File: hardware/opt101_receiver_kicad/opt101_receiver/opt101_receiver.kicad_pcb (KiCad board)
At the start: 2 copper layers, 70 x 32 mm, 11 parts, among them J1 A2 / RED, J2 A0 / IR, J3 ADS1115 outputs, U1 OPT101P, U2 OPT101P

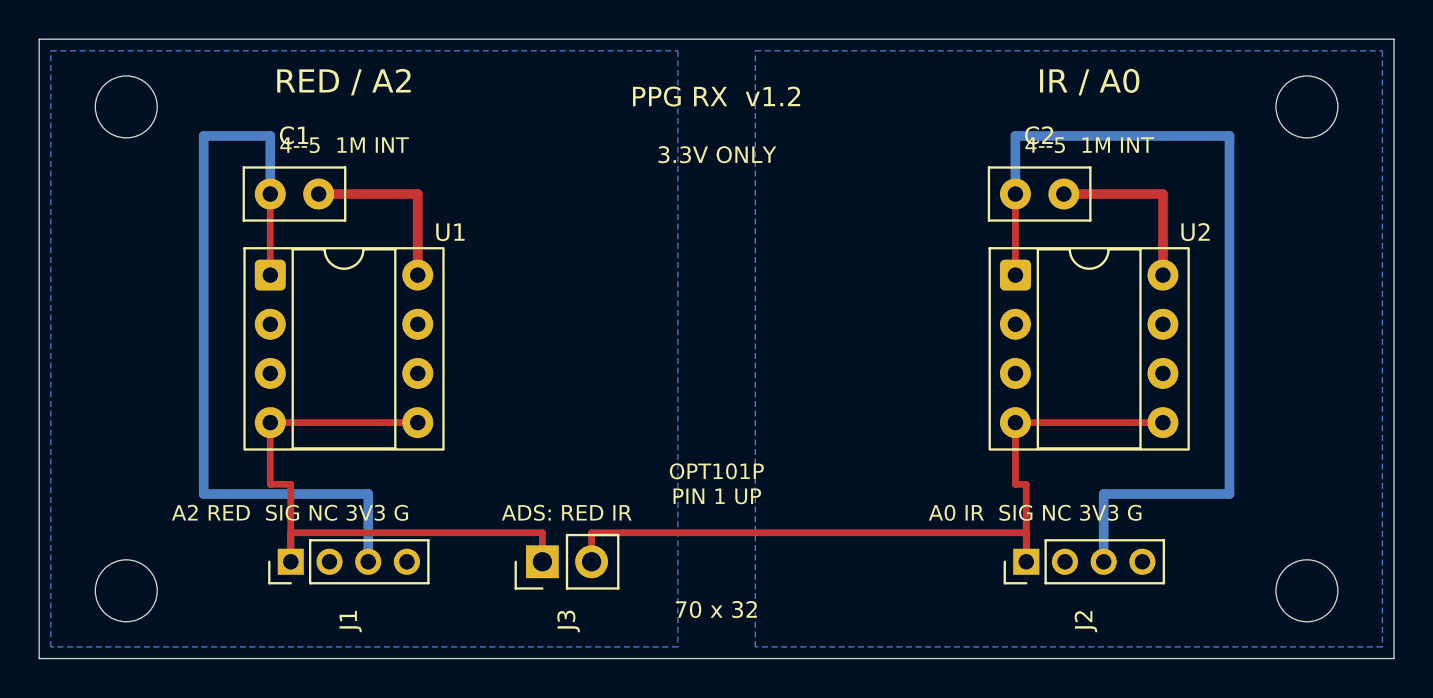
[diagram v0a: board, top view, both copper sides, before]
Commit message: Compact PPG boards, add receiver filters and package V-cut panel
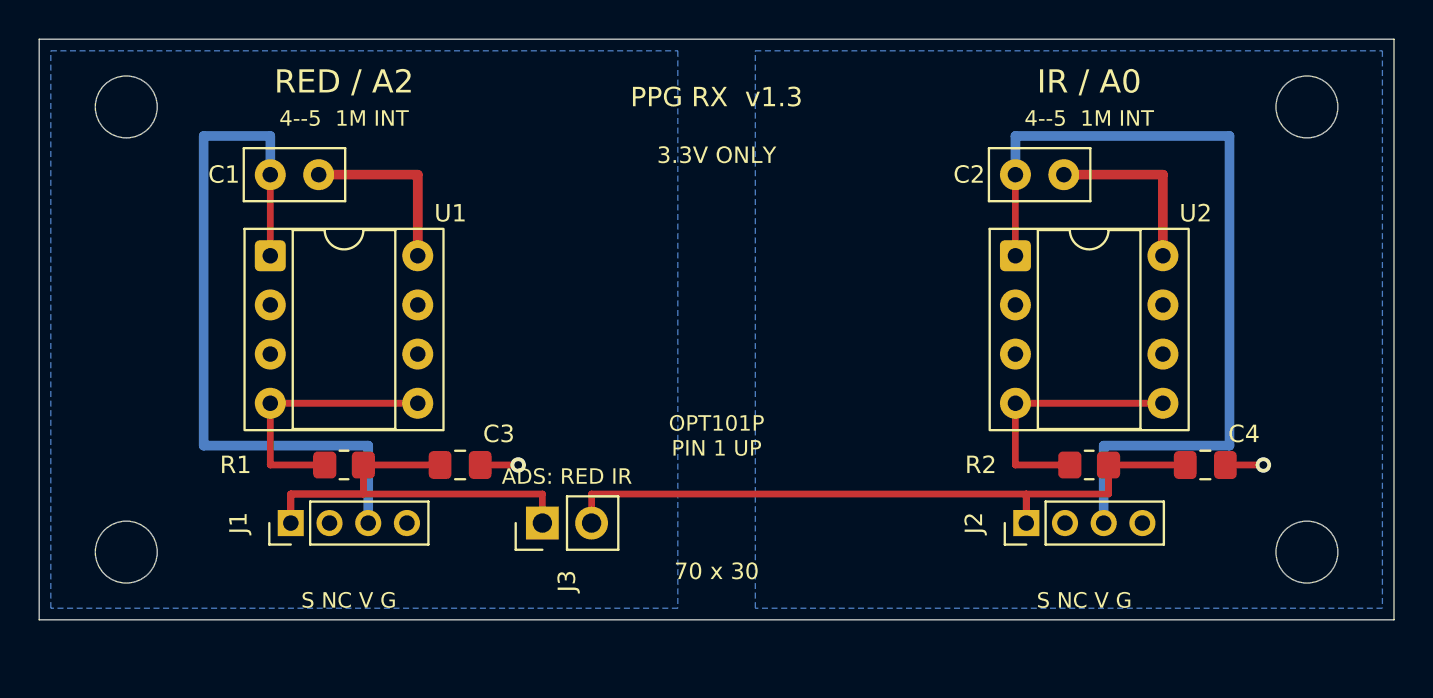
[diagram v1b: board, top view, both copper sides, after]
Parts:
- added C3: 1uF X7R 16V, PPG:C0805_Hand, F.Cu at (121.8, 122.0)
- added C4: 1uF X7R 16V, PPG:C0805_Hand, F.Cu at (160.2, 122.0)
- added R1: 1k 1%, PPG:R0805_Hand, F.Cu at (115.8, 122.0)
- added R2: 1k 1%, PPG:R0805_Hand, F.Cu at (154.2, 122.0)
- moved H3 2.00 mm to (104.5, 126.5)
- moved H4 2.00 mm to (165.5, 126.5)
- moved J1 2.00 mm to (113.0, 125.0)
- moved J2 2.00 mm to (151.0, 125.0)
- moved J3 2.00 mm to (126.0, 125.0)
- moved C1 1.00 mm to (111.9, 107.0)
- moved C2 1.00 mm to (150.4, 107.0)
- moved U1 1.00 mm to (111.9, 111.2)
- moved U2 1.00 mm to (150.4, 111.2)
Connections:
- U1 pad 4: /OUT_RED -> /RAW_RED
- U1 pad 5: /OUT_RED -> /RAW_RED
- U2 pad 4: /OUT_IR -> /RAW_IR
- U2 pad 5: /OUT_IR -> /RAW_IR
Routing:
- net /RAW_RED: track 0.00 -> 13.6 mm
- net /RAW_IR: track 0.00 -> 13.6 mm
- net /OUT_RED: track 31.9 -> 26.7 mm
- net /OUT_IR: track 40.8 -> 36.7 mm
- net /3V3_RED: track 41.1 -> 38.1 mm
- net /3V3_IR: track 46.8 -> 43.8 mm
- net /GND_RED: track 9.31 -> 11.3 mm, vias 0 -> 1
- net /GND_IR: track 9.31 -> 11.3 mm, vias 0 -> 1
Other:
- board size 70 x 32 mm -> 70 x 30 mm
- board text added: "70 x 30"
- board text added: "PPG RX v1.3"
- board text added: "S NC V G"
- board text removed: "70 x 32"
- board text removed: "A0 IR SIG NC 3V3 G"
- board text removed: "A2 RED SIG NC 3V3 G"
- board text removed: "PPG RX v1.2"

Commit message: Convert PPG passives to SMD and refresh compact V-cut panel
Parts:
- C1, C2: footprint PPG:Bypass_100n_P2.5mm -> PPG:C0805_Hand
- moved C1 1.25 mm to (113.2, 107.0)
- moved C2 1.25 mm to (151.7, 107.0)
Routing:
- net /3V3_RED: track 38.1 -> 38.3 mm, vias 0 -> 1
- net /3V3_IR: track 43.8 -> 44.0 mm, vias 0 -> 1
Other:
- board text added: "PPG RX v1.4"
- board text removed: "PPG RX v1.3"

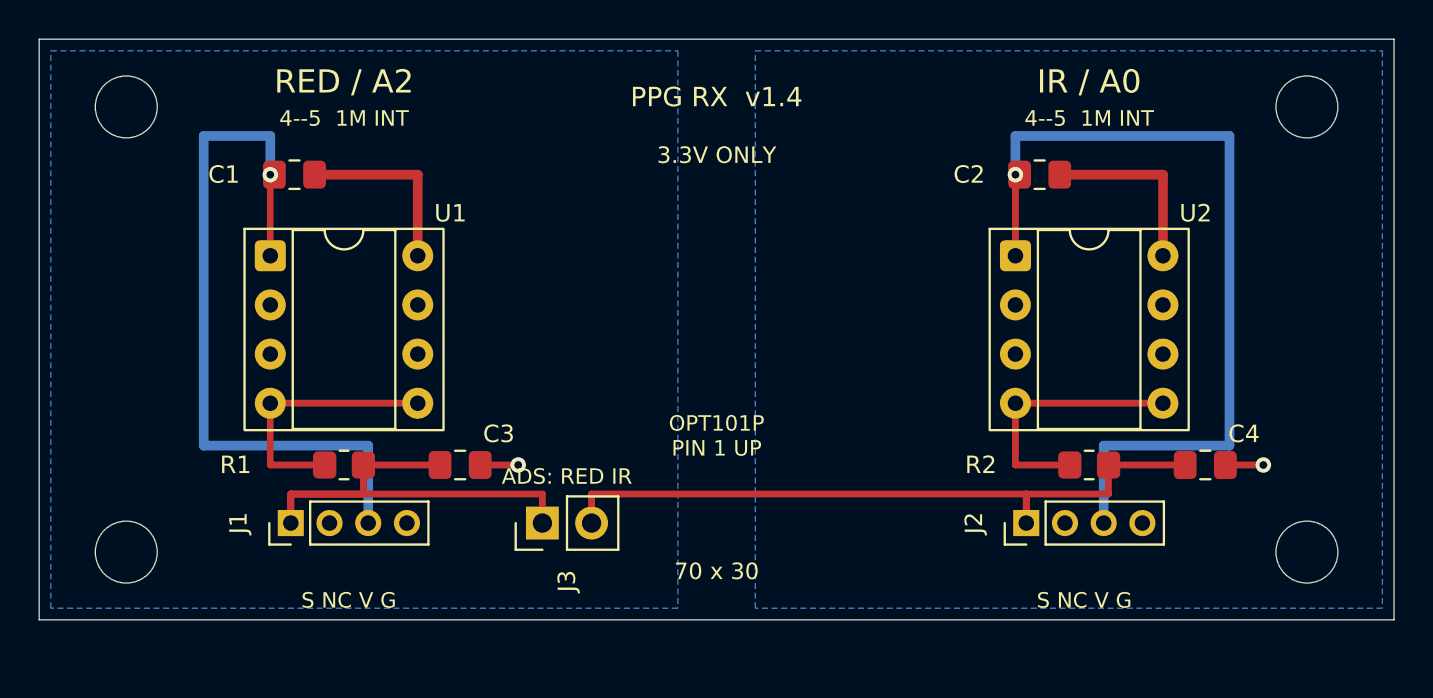
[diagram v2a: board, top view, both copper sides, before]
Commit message: Shrink PPG receivers to 70x20 and driver to 70x40; refresh V-cut release
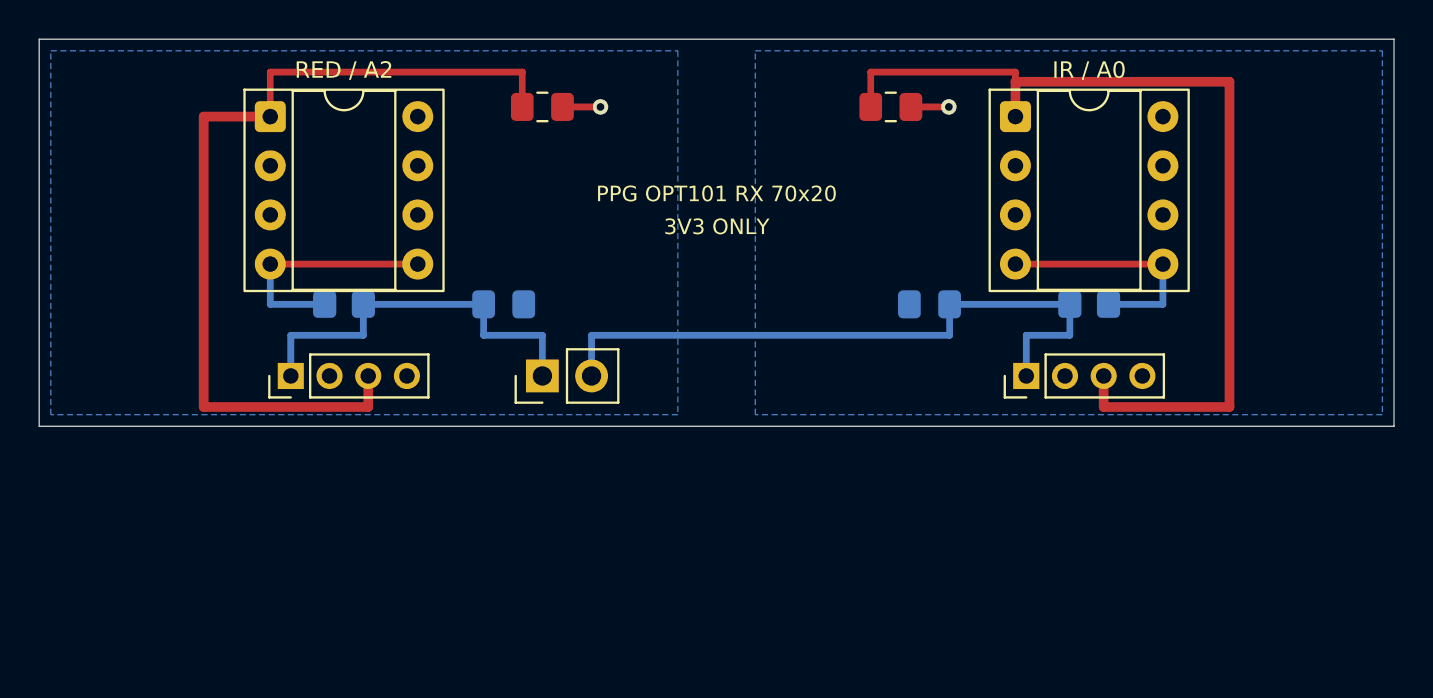
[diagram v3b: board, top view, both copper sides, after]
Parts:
- removed H1, H2, H3, H4: M3 / 3.2mm NPTH, PPG:MountingHole_M3
- C3, C4, R1, R2: moved to B.Cu
- moved C4 16.5 mm to (146.0, 113.7), turned to 180 degrees
- moved C1 13.3 mm to (126.0, 103.5)
- moved C3 8.60 mm to (124.0, 113.7)
- moved C2 8.45 mm to (144.0, 103.5)
- moved R1 8.30 mm to (115.8, 113.7)
- moved R2 8.30 mm to (154.2, 113.7), turned to 180 degrees
- moved J1 7.60 mm to (113.0, 117.4)
- moved J2 7.60 mm to (151.0, 117.4)
- moved J3 7.60 mm to (126.0, 117.4)
- moved U1 7.19 mm to (111.9, 104.0)
- moved U2 7.19 mm to (150.4, 104.0)
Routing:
- net /GND_IR: track 11.5 -> 1.96 mm
- net /GND_RED: track 11.5 -> 1.96 mm
- net /3V3_RED: track 38.3 -> 45.7 mm, vias 1 -> 0
- net /OUT_RED: track 26.7 -> 20.4 mm
- net /3V3_IR: track 44.0 -> 49.3 mm, vias 1 -> 0
- net /OUT_IR: track 36.7 -> 34.4 mm
- net /RAW_RED: track 13.6 -> 12.5 mm
- net /RAW_IR: track 13.6 -> 12.5 mm
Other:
- board size 70 x 30 mm -> 70 x 20 mm
- board text added: "3V3 ONLY"
- board text added: "PPG OPT101 RX 70x20"
- board text added: "S"
- board text removed: "3.3V ONLY"
- board text removed: "4--5 1M INT"
- board text removed: "70 x 30"
- board text removed: "ADS: RED IR"
- board text removed: "GI"
- board text removed: "GR"
- board text removed: "J1 A2 RED"
- board text removed: "J2 A0 IR"
- board text removed: "J3 ADS"
- board text removed: "OPT101P PIN 1 UP"
- board text removed: "PPG RX v1.4"
- board text removed: "R=OUT_RED I=OUT_IR"
- board text removed: "S NC V G"
- board text removed: "U1 RED OPT101"
- board text removed: "U2 IR OPT101"
- board text removed: "V=3V3 GR/GI=GND"

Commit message: Increase V-score copper and component margins; reposition receiver circuits
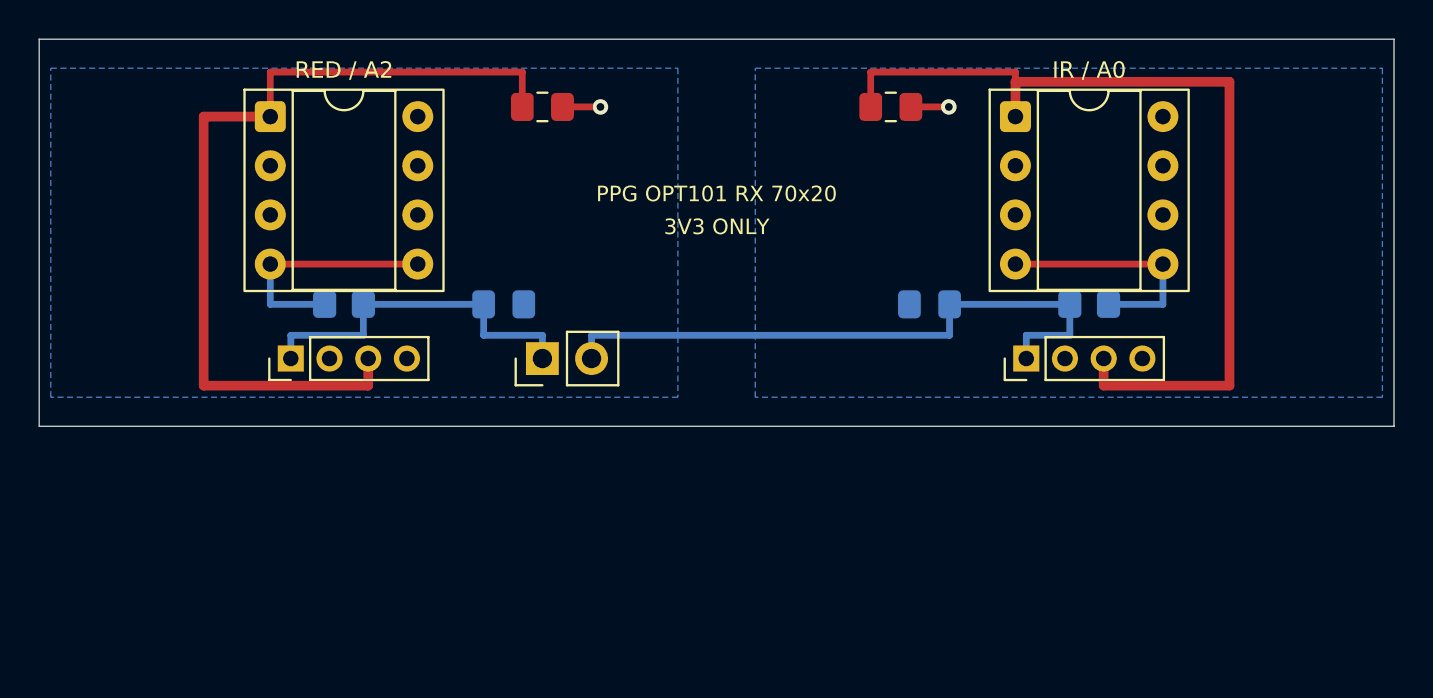
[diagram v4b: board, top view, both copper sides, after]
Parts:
- moved J1 0.90 mm to (113.0, 116.5)
- moved J2 0.90 mm to (151.0, 116.5)
- moved J3 0.90 mm to (126.0, 116.5)
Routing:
- net /OUT_RED: track 20.4 -> 18.6 mm
- net /OUT_IR: track 34.4 -> 32.6 mm
- net /3V3_RED: track 45.7 -> 44.4 mm
- net /3V3_IR: track 49.3 -> 48.0 mm

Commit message: Chamfer PPG board routing to 45 degrees and verify V-score fabrication release
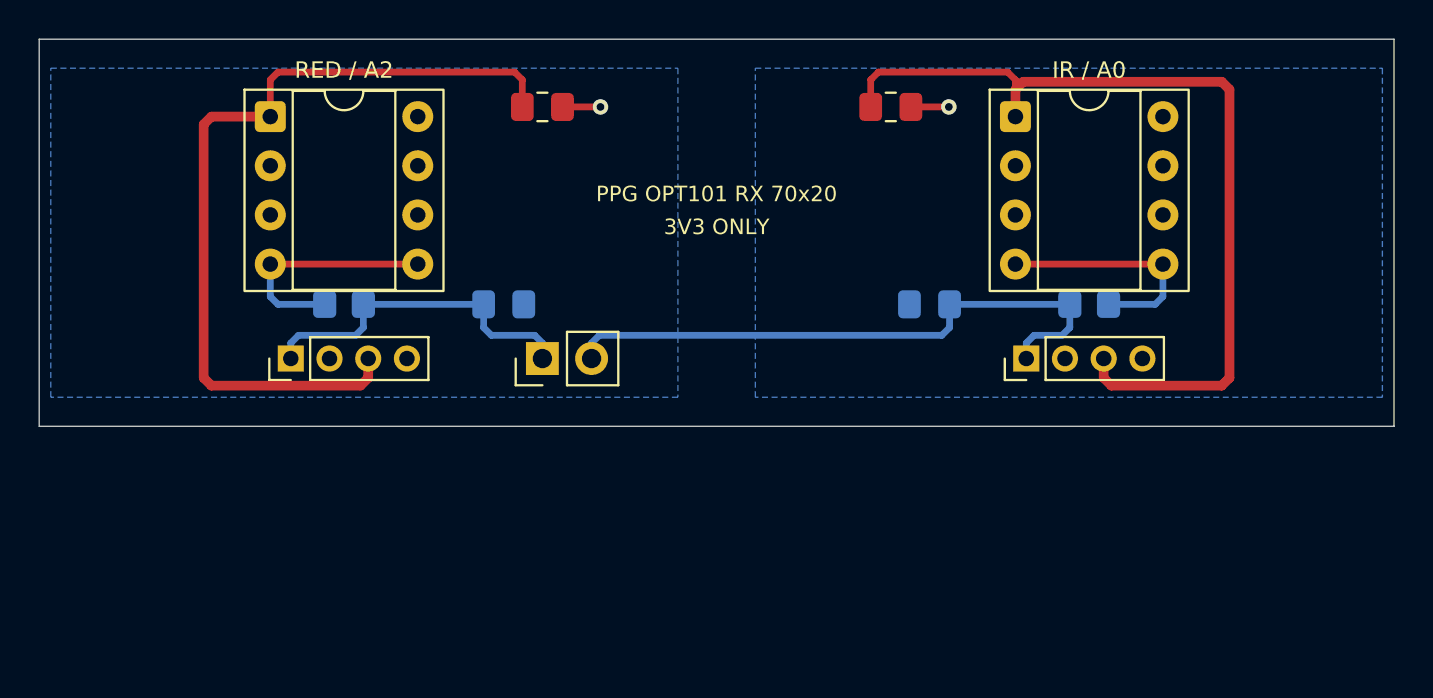
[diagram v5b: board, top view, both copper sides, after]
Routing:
- net /3V3_IR: track 48.0 -> 46.6 mm
- net /3V3_RED: track 44.4 -> 43.2 mm
- net /OUT_RED: track 18.6 -> 17.7 mm
- net /OUT_IR: track 32.6 -> 31.6 mm

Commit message: Lengthen 45-degree PCB bends and refresh fabrication packages
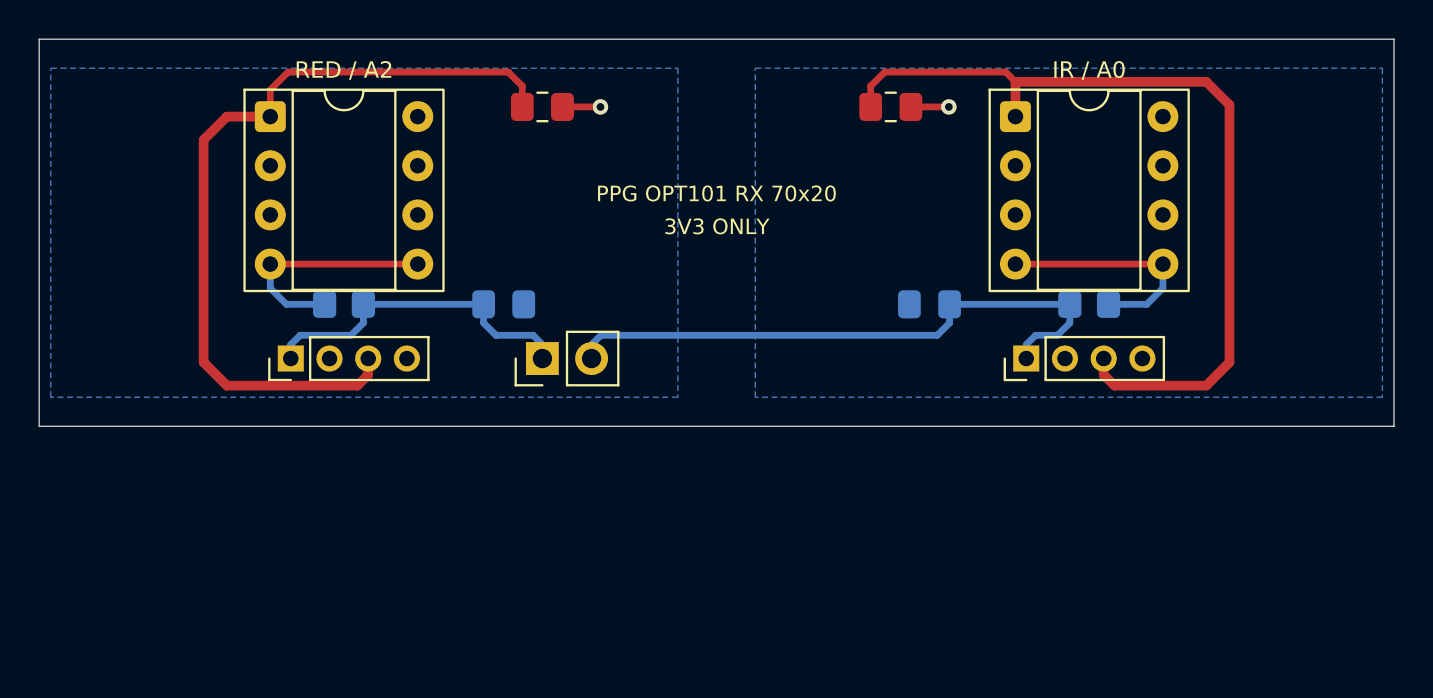
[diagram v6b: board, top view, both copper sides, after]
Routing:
- net /3V3_RED: track 43.2 -> 41.7 mm
- net /3V3_IR: track 46.6 -> 45.6 mm

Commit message: Update README.md, hardware 45-degree routing and OPT101 diagnostic docs
- Fix version line in README.md to ensure version consistency test passes
- Document persistent live A0/A2 RX monitor dock and touch UI scaling
- Document OPT101 physical bench diagnostic protocol (docs/opt101-a0-diagnostic-2026-10-01.md)
- Detail 45-degree chamfered PCB routing, segment cleanup, and updated wiring guides
- Update repository tree and refreshed manufacturing release ZIPs
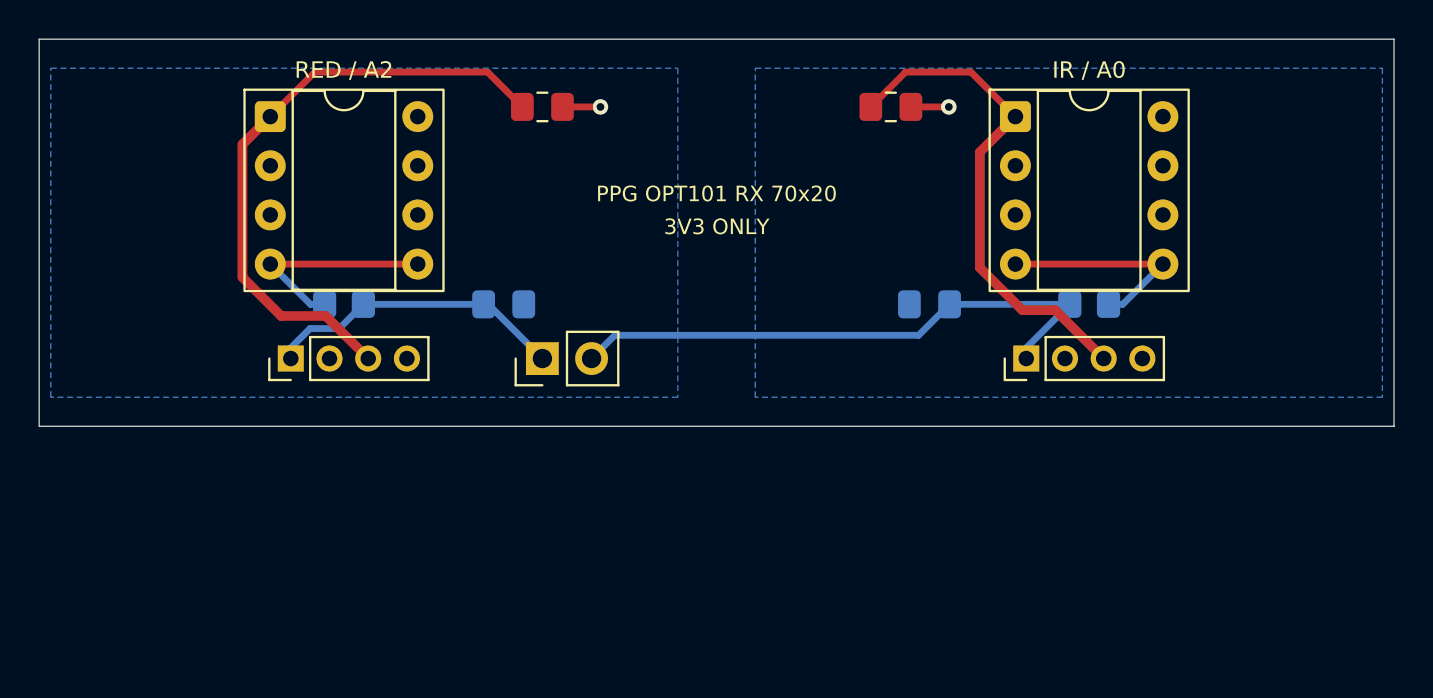
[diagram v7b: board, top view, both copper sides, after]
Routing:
- net /3V3_IR: track 45.6 -> 26.1 mm
- net /3V3_RED: track 41.7 -> 31.9 mm
- net /OUT_IR: track 31.2 -> 29.6 mm
- net /OUT_RED: track 17.3 -> 15.6 mm
- net /RAW_IR: track 12.0 -> 11.3 mm
- net /RAW_RED: track 12.0 -> 11.3 mm
